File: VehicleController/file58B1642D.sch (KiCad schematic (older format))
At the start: 40 parts, among them J8 CONN_01X03, J9 CONN_02X12, Q4 Q_NMOS_GDS, Q5 PC_FET, Q6 PC_FET, U16 MC_Override, U17 MCR_Shtdwn, U18 MCL_Shtdwn, U19 RI-0505S, U20 ISO1540, U21 TCMT1103, U22 OPTO-TRANSISTOR-4, U23 PC_RLY, U24 MCP47FEBX2

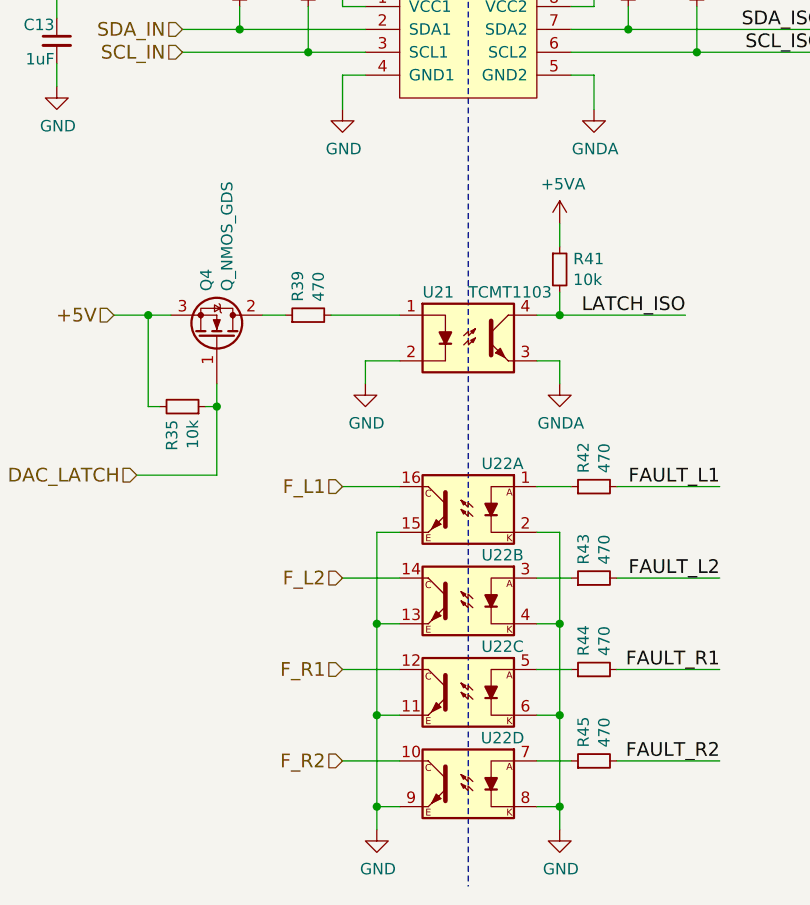
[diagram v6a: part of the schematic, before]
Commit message: Decoupling updates, small VCU changes
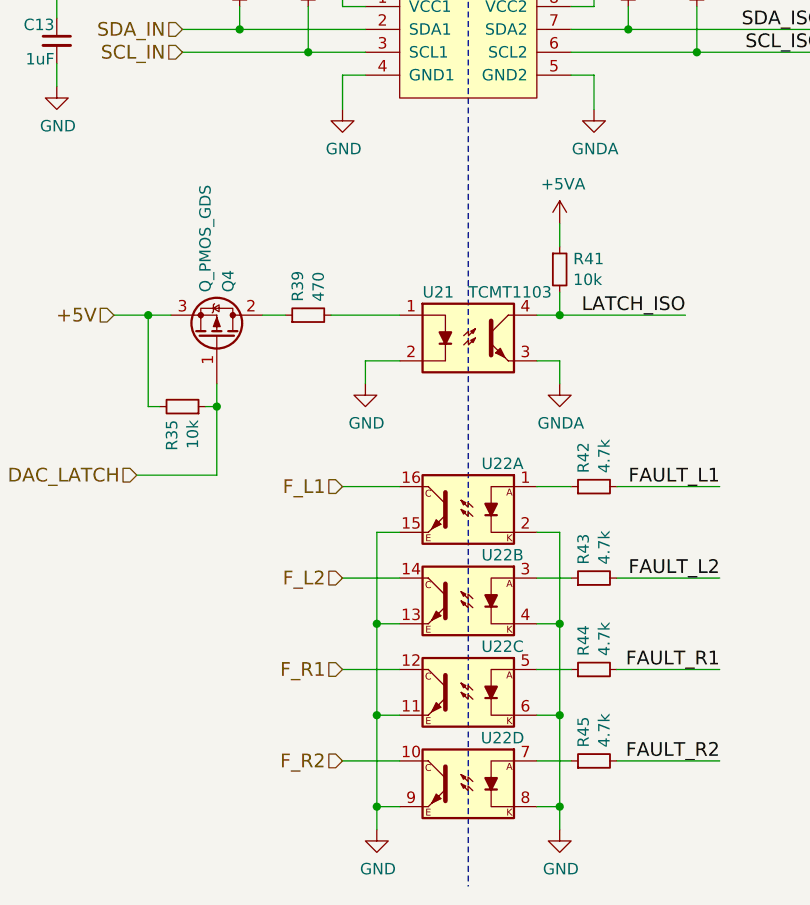
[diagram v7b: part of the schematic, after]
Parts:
- removed Q4: Q_NMOS_GDS, TO_SOT_Packages_SMD:SOT-23_Handsoldering, symbol Q_NMOS_GDS
- added Q4: Q_PMOS_GDS, symbol Q_PMOS_GDS
- R42, R43, R44, R45: value 470 -> 4.7k
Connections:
- net +5V: now also Q4.3 (S)
- net DAC_LATCH: now also Q4.1 (G)
- net at R39.1: now also Q4.2 (D)
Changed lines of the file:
@@
 $EndComp
 $Comp
-L +5VA #PWR070
+L +5VA #PWR83
 U 1 1 58B166C2
 P 7850 6250
-F 0 "#PWR070" H 7850 6100 50  0001 C CNN
+F 0 "#PWR83" H 7850 6100 50  0001 C CNN
 F 1 "+5VA" H 7865 6423 50  0000 C CNN
 F 2 "" H 7850 6250 50  0000 C CNN
@@
 $EndComp
 $Comp
-L GNDA #PWR071
+L GNDA #PWR84
 U 1 1 58B166E6
 P 7850 7000
-F 0 "#PWR071" H 7850 6750 50  0001 C CNN
+F 0 "#PWR84" H 7850 6750 50  0001 C CNN
 F 1 "GNDA" H 7855 6827 50  0000 C CNN
 F 2 "" H 7850 7000 50  0000 C CNN
@@
 $EndComp
 $Comp
-L GND #PWR072
+L GND #PWR74
 U 1 1 58B166F7
 P 6750 7000
-F 0 "#PWR072" H 6750 6750 50  0001 C CNN
+F 0 "#PWR74" H 6750 6750 50  0001 C CNN
 F 1 "GND" H 6755 6827 50  0000 C CNN
 F 2 "" H 6750 7000 50  0000 C CNN
@@
 $EndComp
 $Comp
-L +5VA #PWR073
+L +5VA #PWR81
 U 1 1 58B17364
 P 7850 5350
-F 0 "#PWR073" H 7850 5200 50  0001 C CNN
+F 0 "#PWR81" H 7850 5200 50  0001 C CNN
 F 1 "+5VA" H 7865 5523 50  0000 C CNN
 F 2 "" H 7850 5350 50  0000 C CNN
@@
 $EndComp
 $Comp
-L GNDA #PWR074
+L GNDA #PWR82
 U 1 1 58B173AF
 P 7850 5800
-F 0 "#PWR074" H 7850 5550 50  0001 C CNN
+F 0 "#PWR82" H 7850 5550 50  0001 C CNN
 F 1 "GNDA" H 7855 5627 50  0000 C CNN
 F 2 "" H 7850 5800 50  0000 C CNN
@@
 $EndComp
 $Comp
-L GNDA #PWR075
+L GNDA #PWR79
 U 1 1 58B17D44
 P 7700 8200
-F 0 "#PWR075" H 7700 7950 50  0001 C CNN
+F 0 "#PWR79" H 7700 7950 50  0001 C CNN
 F 1 "GNDA" H 7705 8027 50  0000 C CNN
 F 2 "" H 7700 8200 50  0000 C CNN
@@
 NoConn ~ 12500 6000
 $Comp
-L GNDA #PWR076
+L GNDA #PWR90
 U 1 1 58B181A1
 P 10750 6100
-F 0 "#PWR076" H 10750 5850 50  0001 C CNN
+F 0 "#PWR90" H 10750 5850 50  0001 C CNN
 F 1 "GNDA" H 10755 5927 50  0000 C CNN
 F 2 "" H 10750 6100 50  0000 C CNN
@@
 $EndComp
 $Comp
-L +5VA #PWR077
+L +5VA #PWR89
 U 1 1 58B181A7
 P 10750 5500
-F 0 "#PWR077" H 10750 5350 50  0001 C CNN
+F 0 "#PWR89" H 10750 5350 50  0001 C CNN
 F 1 "+5VA" H 10765 5673 50  0000 C CNN
 F 2 "" H 10750 5500 50  0000 C CNN
@@
 $EndComp
 $Comp
-L +5VA #PWR078
+L +5VA #PWR78
 U 1 1 58B1875A
 P 7700 7500
-F 0 "#PWR078" H 7700 7350 50  0001 C CNN
+F 0 "#PWR78" H 7700 7350 50  0001 C CNN
 F 1 "+5VA" H 7715 7673 50  0000 C CNN
 F 2 "" H 7700 7500 50  0000 C CNN
@@
 SCL_IN
 $Comp
-L GND #PWR079
+L GND #PWR72
 U 1 1 58B1731B
 P 6750 5700
-F 0 "#PWR079" H 6750 5450 50  0001 C CNN
+F 0 "#PWR72" H 6750 5450 50  0001 C CNN
 F 1 "GND" H 6755 5527 50  0000 C CNN
 F 2 "" H 6750 5700 50  0000 C CNN
@@
 $EndComp
 $Comp
-L +5V #PWR080
+L +5V #PWR71
 U 1 1 58B172D4
 P 6750 5300
-F 0 "#PWR080" H 6750 5150 50  0001 C CNN
+F 0 "#PWR71" H 6750 5150 50  0001 C CNN
 F 1 "+5V" H 6765 5473 50  0000 C CNN
 F 2 "" H 6750 5300 50  0000 C CNN
@@
 DAC_LATCH
 $Comp
-L +5V #PWR081
+L +5V #PWR73
 U 1 1 58B166EE
 P 6750 6200
-F 0 "#PWR081" H 6750 6050 50  0001 C CNN
+F 0 "#PWR73" H 6750 6050 50  0001 C CNN
 F 1 "+5V" H 6765 6373 50  0000 C CNN
 F 2 "" H 6750 6200 50  0000 C CNN
@@
 CONTACT_R
 $Comp
-L GNDA #PWR082
+L GNDA #PWR91
 U 1 1 58BA1834
 P 11550 4650
-F 0 "#PWR082" H 11550 4400 50  0001 C CNN
+F 0 "#PWR91" H 11550 4400 50  0001 C CNN
 F 1 "GNDA" H 11555 4477 50  0000 C CNN
 F 2 "" H 11550 4650 50  0000 C CNN
@@
 CONTACT_L
 $Comp
-L GNDA #PWR083
+L GNDA #PWR92
 U 1 1 58BA3088
 P 12250 4650
-F 0 "#PWR083" H 12250 4400 50  0001 C CNN
+F 0 "#PWR92" H 12250 4400 50  0001 C CNN
 F 1 "GNDA" H 12255 4477 50  0000 C CNN
 F 2 "" H 12250 4650 50  0000 C CNN
@@
 $EndComp
 $Comp
-L GND #PWR084
+L GND #PWR77
 U 1 1 58BB11C1
 P 7200 2100
-F 0 "#PWR084" H 7200 1850 50  0001 C CNN
+F 0 "#PWR77" H 7200 1850 50  0001 C CNN
 F 1 "GND" H 7205 1927 50  0000 C CNN
 F 2 "" H 7200 2100 50  0000 C CNN
@@
 $EndComp
 $Comp
-L GNDA #PWR085
+L GNDA #PWR86
 U 1 1 58C41861
 P 9100 5550
-F 0 "#PWR085" H 9100 5300 50  0001 C CNN
+F 0 "#PWR86" H 9100 5300 50  0001 C CNN
 F 1 "GNDA" H 9105 5377 50  0000 C CNN
 F 2 "" H 9100 5550 50  0000 C CNN
@@
 $EndComp
 $Comp
-L Q_NMOS_GDS Q4
-U 1 1 58C4E642
-P 6200 8000
-F 0 "Q4" H 6405 7954 50  0000 L CNN
-F 1 "Q_NMOS_GDS" H 6405 8045 50  0000 L CNN
-F 2 "TO_SOT_Packages_SMD:SOT-23_Handsoldering" H 500 300 50  0001 C CNN
-F 3 "" H 300 200 50  0001 C CNN
-	1    6200 8000
-	0    1    -1   0
-$EndComp
-$Comp
-L GND #PWR086
+L GND #PWR75
 U 1 1 58C501B1
 P 6850 8200
-F 0 "#PWR086" H 6850 7950 50  0001 C CNN
+F 0 "#PWR75" H 6850 7950 50  0001 C CNN
 F 1 "GND" H 6855 8027 50  0000 C CNN
 F 2 "" H 6850 8200 50  0000 C CNN
@@
 FAULT_R2
 $Comp
-L GND #PWR087
+L GND #PWR80
 U 1 1 58CAFC96
 P 7700 10150
-F 0 "#PWR087" H 7750 10200 50  0001 C CNN
+F 0 "#PWR80" H 7750 10200 50  0001 C CNN
 F 1 "GND" H 7705 9977 50  0000 C CNN
 F 2 "" H -700 1050 50  0001 C CNN
@@
 F_R2
 $Comp
-L GND #PWR088
+L GND #PWR76
 U 1 1 58CA2742
 P 6900 10150
-F 0 "#PWR088" H 6950 10200 50  0001 C CNN
+F 0 "#PWR76" H 6950 10200 50  0001 C CNN
 F 1 "GND" H 6905 9977 50  0000 C CNN
 F 2 "" H -1500 1050 50  0001 C CNN
@@
 KSI
 $Comp
-L GNDA #PWR089
+L GNDA #PWR85
 U 1 1 590261A6
 P 8400 1050
-F 0 "#PWR089" H 8400 800 50  0001 C CNN
+F 0 "#PWR85" H 8400 800 50  0001 C CNN
 F 1 "GNDA" H 8405 877 50  0000 C CNN
 F 2 "" H 8400 1050 50  0000 C CNN
@@
 P 7850 8650
 F 0 "R42" H 7909 8696 50  0000 L CNN
-F 1 "470" H 7909 8605 50  0000 L CNN
+F 1 "4.7k" H 7909 8605 50  0000 L CNN
 F 2 "Resistors_SMD:R_0805_HandSoldering" H 7850 8650 50  0001 C CNN
 F 3 "" H 7850 8650 50  0000 C CNN
@@
 P 7850 9050
 F 0 "R43" H 7909 9096 50  0000 L CNN
-F 1 "470" H 7909 9005 50  0000 L CNN
+F 1 "4.7k" H 7909 9005 50  0000 L CNN
 F 2 "Resistors_SMD:R_0805_HandSoldering" H 7850 9050 50  0001 C CNN
 F 3 "" H 7850 9050 50  0000 C CNN
@@
 P 7850 9450
 F 0 "R44" H 7909 9496 50  0000 L CNN
-F 1 "470" H 7909 9405 50  0000 L CNN
+F 1 "4.7k" H 7909 9405 50  0000 L CNN
 F 2 "Resistors_SMD:R_0805_HandSoldering" H 7850 9450 50  0001 C CNN
 F 3 "" H 7850 9450 50  0000 C CNN
@@
 P 7850 9850
 F 0 "R45" H 7909 9896 50  0000 L CNN
-F 1 "470" H 7909 9805 50  0000 L CNN
+F 1 "4.7k" H 7909 9805 50  0000 L CNN
 F 2 "Resistors_SMD:R_0805_HandSoldering" H 7850 9850 50  0001 C CNN
 F 3 "" H 7850 9850 50  0000 C CNN
@@
 $EndComp
 $Comp
-L +5V #PWR090
+L +5V #PWR67
 U 1 1 59116008
 P 5500 6500
-F 0 "#PWR090" H 5500 6350 50  0001 C CNN
+F 0 "#PWR67" H 5500 6350 50  0001 C CNN
 F 1 "+5V" H 5515 6673 50  0000 C CNN
 F 2 "" H 5500 6500 50  0000 C CNN
@@
 $EndComp
 $Comp
-L GND #PWR091
+L GND #PWR68
 U 1 1 5911608E
 P 5500 6900
-F 0 "#PWR091" H 5500 6650 50  0001 C CNN
+F 0 "#PWR68" H 5500 6650 50  0001 C CNN
 F 1 "GND" H 5505 6727 50  0000 C CNN
 F 2 "" H 5500 6900 50  0000 C CNN
@@
 $EndComp
 $Comp
-L +5VA #PWR092
+L +5VA #PWR87
 U 1 1 591164A6
 P 9100 6500
-F 0 "#PWR092" H 9100 6350 50  0001 C CNN
+F 0 "#PWR87" H 9100 6350 50  0001 C CNN
 F 1 "+5VA" H 9115 6673 50  0000 C CNN
 F 2 "" H 9100 6500 50  0000 C CNN
@@
 	9100 6500 9100 6600
 $Comp
-L GNDA #PWR093
+L GNDA #PWR88
 U 1 1 5911666B
 P 9100 6900
-F 0 "#PWR093" H 9100 6650 50  0001 C CNN
+F 0 "#PWR88" H 9100 6650 50  0001 C CNN
 F 1 "GNDA" H 9105 6727 50  0000 C CNN
 F 2 "" H 9100 6900 50  0000 C CNN
@@
 	6650 3450 6650 3600
 $Comp
-L GND #PWR094
+L GND #PWR70
 U 1 1 591496EE
 P 6650 4150
-F 0 "#PWR094" H 6650 3900 50  0001 C CNN
+F 0 "#PWR70" H 6650 3900 50  0001 C CNN
 F 1 "GND" H 6655 3977 50  0000 C CNN
 F 2 "" H 6650 4150 50  0000 C CNN
@@
 Connection ~ 6250 3800
 $Comp
-L +5V #PWR095
+L +5V #PWR69
 U 1 1 5914B610
 P 6650 2950
-F 0 "#PWR095" H 6650 2800 50  0001 C CNN
+F 0 "#PWR69" H 6650 2800 50  0001 C CNN
 F 1 "+5V" H 6650 3090 50  0000 C CNN
 F 2 "" H 6650 2950 50  0001 C CNN
@@
 	5850 3500 6650 3500
 Connection ~ 6650 3500
+$Comp
+L Q_PMOS_GDS Q4
+U 1 1 590A4446
+P 6200 8000
+F 0 "Q4" H 6400 8050 50  0000 L CNN
+F 1 "Q_PMOS_GDS" H 6400 7950 50  0000 L CNN
+F 2 "" H 6400 8100 50  0001 C CNN
+F 3 "" H 6200 8000 50  0001 C CNN
+	1    6200 8000
+	0    1    -1   0
+$EndComp
 $EndSCHEMATC

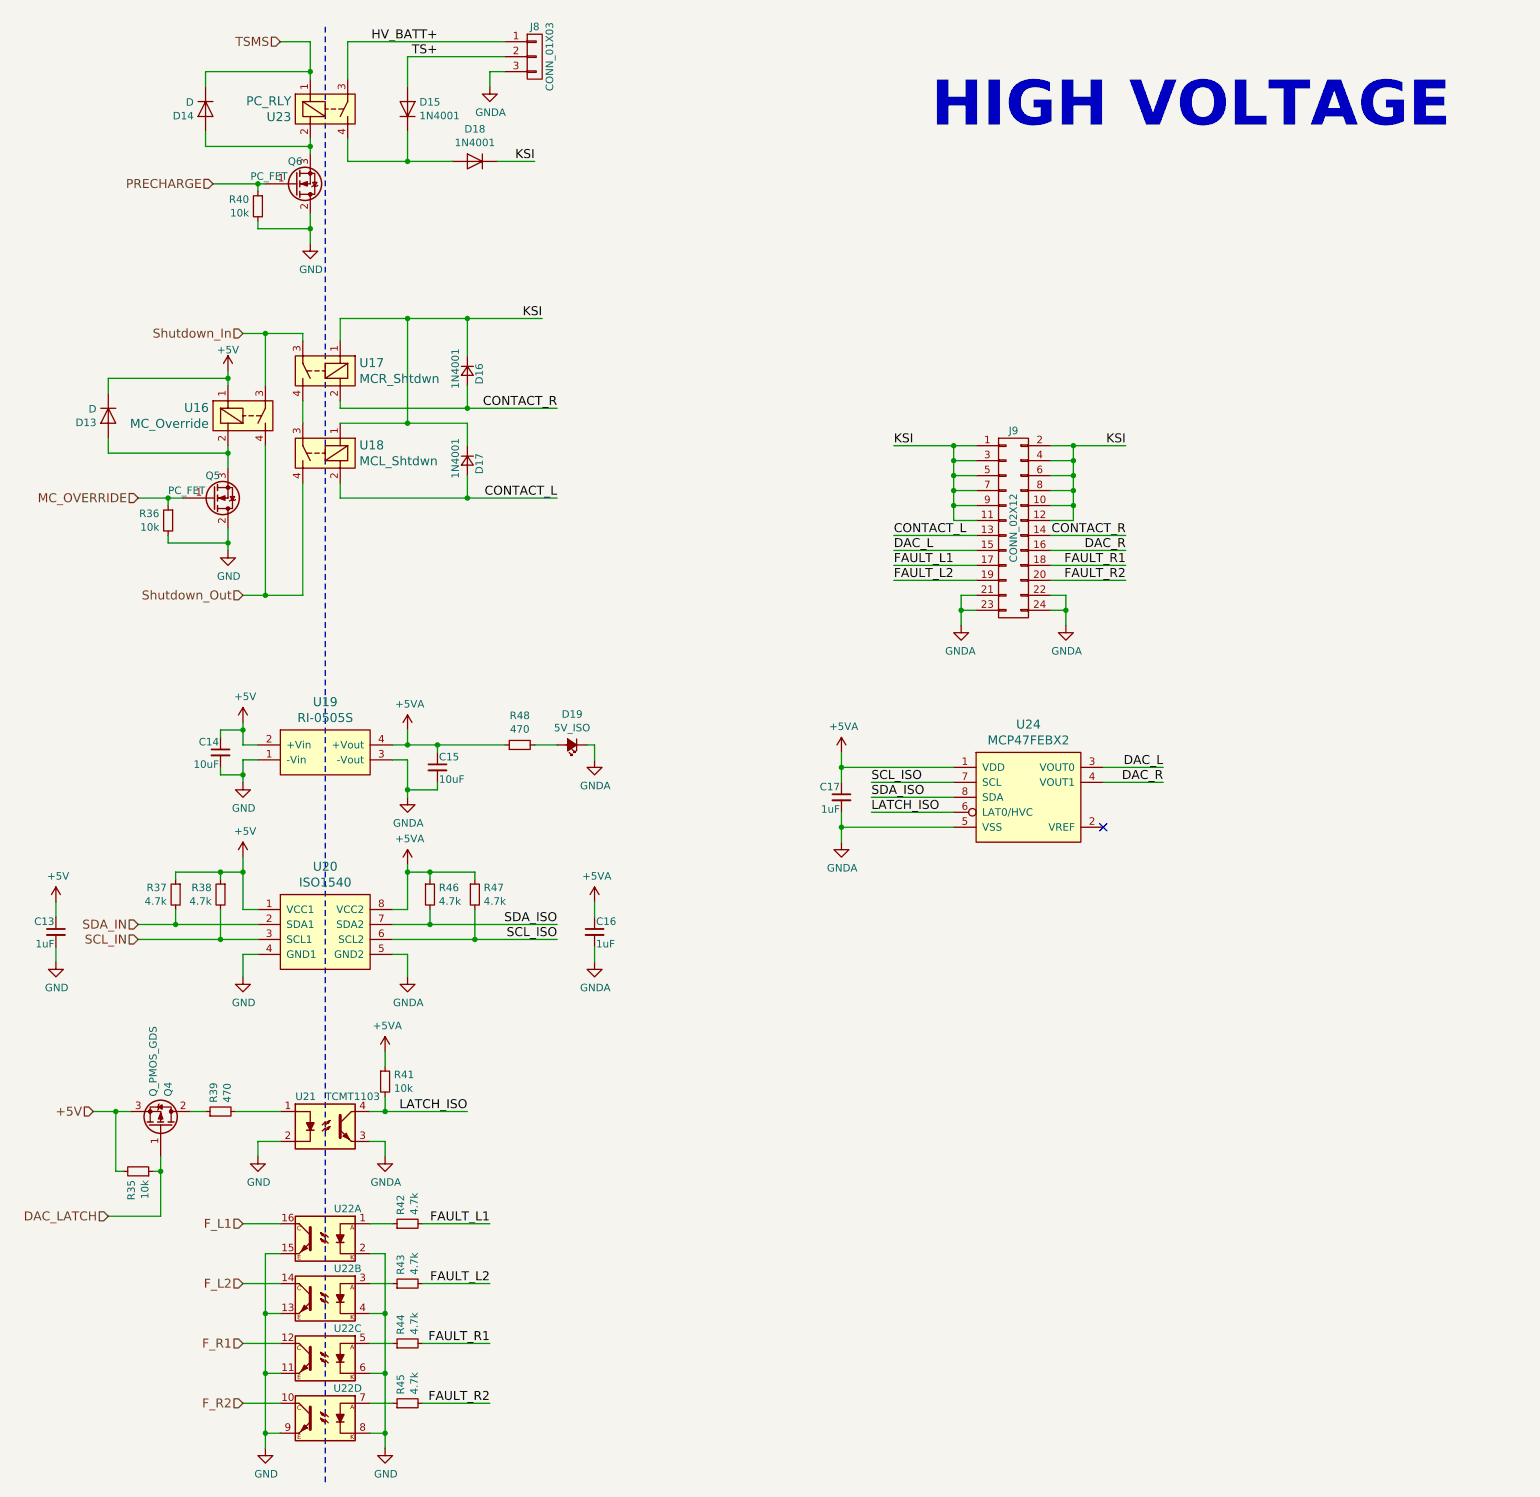
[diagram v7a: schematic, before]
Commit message: MX120, GDS->GSD FETs on VCU
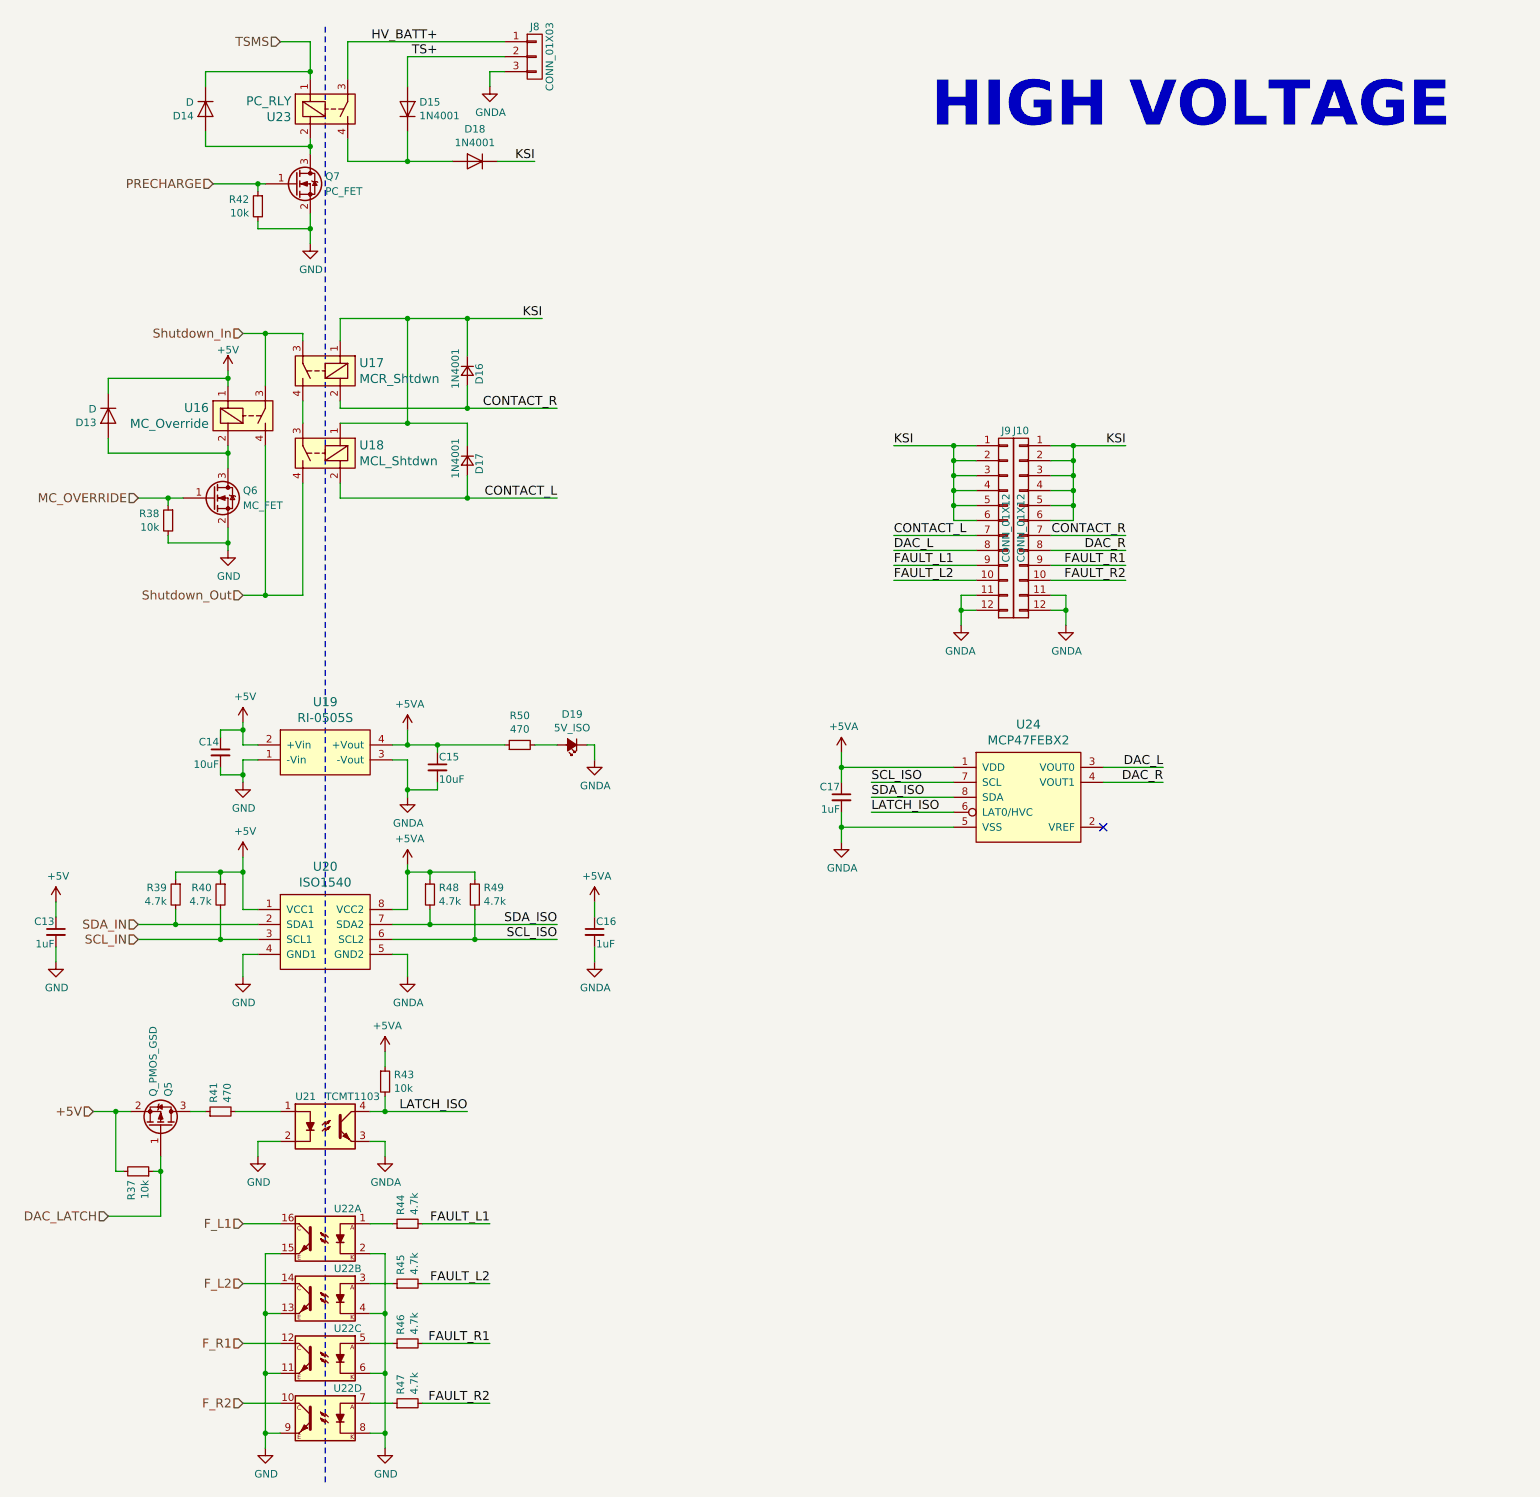
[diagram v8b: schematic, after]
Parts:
- removed J9: CONN_02X12, symbol CONN_02X12
- removed Q4: Q_PMOS_GDS, symbol Q_PMOS_GDS
- removed Q5, Q6: PC_FET, TO_SOT_Packages_SMD:SOT-23_Handsoldering, symbol Q_NMOS_GDS
- added J10, J9: CONN_01X12, UNCA Motorsports:MX120G-12, symbol CONN_01X12
- added Q5: Q_PMOS_GSD, TO_SOT_Packages_SMD:SOT-23_Handsoldering, symbol Q_PMOS_GSD
- added Q6: MC_FET, TO_SOT_Packages_SMD:SOT-23_Handsoldering, symbol Q_NMOS_GSD
- added Q7: PC_FET, TO_SOT_Packages_SMD:SOT-23_Handsoldering, symbol Q_NMOS_GSD
- D13, D14, D15, D18: footprint Diodes_SMD:SMA_Handsoldering -> Diodes_SMD:D_SMC_Handsoldering
- D16, D17: footprint (none) -> Diodes_SMD:D_SMC_Handsoldering
- J8: footprint (none) -> Pin_Headers:Pin_Header_Straight_1x03_Pitch2.54mm
- U22: value OPTO-TRANSISTOR-4 -> TLP293-4; footprint (none) -> UNCA Motorsports:SOIC16
- renumbered R35 to R37, R36 to R38, R37 to R39, R38 to R40, R39 to R41, R40 to R42, R41 to R43, R42 to R44, R43 to R45, R44 to R46, R45 to R47, R46 to R48, R47 to R49, R48 to R50
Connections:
- net +5V: now also Q5.2 (S)
- net CONTACT_L: now also J9.7 (P7)
- net CONTACT_R: now also J10.7 (P7)
- net DAC_L: now also J9.8 (P8)
- net DAC_LATCH: now also Q5.1 (G)
- net DAC_R: now also J10.8 (P8)
- net FAULT_L1: now also J9.9 (P9)
- net FAULT_L2: now also J9.10 (P10)
- net FAULT_R1: now also J10.9 (P9)
- net FAULT_R2: now also J10.10 (P10)
- net GND: now also Q6.2 (S), Q7.2 (S)
- net GNDA: now also J10.11 (P11), J10.12 (P12), J9.11 (P11), J9.12 (P12)
- net KSI: now also J10.1 (P1), J10.2 (P2), J10.3 (P3), J10.4 (P4), J10.5 (P5), J10.6 (P6), J9.1 (P1), J9.2 (P2), J9.3 (P3), J9.4 (P4), J9.5 (P5), J9.6 (P6)
- net MC_OVERRIDE: now also Q6.1 (G)
- net PRECHARGE: now also Q7.1 (G)
- net at R41.1: now also Q5.3 (D)
- net at D14.2 (A), U23.2: now also Q7.3 (D)
- net at D13.2 (A), U16.2: now also Q6.3 (D)
